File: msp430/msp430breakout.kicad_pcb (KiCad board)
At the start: 2 copper layers, 17 parts, among them P1 Power, X1 Power, X2 Power, X3 Left, X4 Power, X5 Power, X6 Right, X7 Debug

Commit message: a bit of work on the layout
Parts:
- added X8: PWR_L_OOL, Connector_PinHeader_2.54mm:PinHeader_2x02_P2.54mm_Vertical, B.Cu at (127.1, 101.3)
- added X9: PWR_R_OOL, Connector_PinHeader_2.54mm:PinHeader_2x02_P2.54mm_Vertical, B.Cu at (170.3, 101.3)
- C3: moved to B.Cu
- R1, R2: moved to F.Cu
- X3, X6: footprint Connector_PinHeader_2.54mm:PinHeader_1x06_P2.54mm_Vertical -> Connector_PinHeader_2.54mm:PinHeader_1x05_P2.54mm_Vertical
- X7: footprint Connector_Molex:Molex_Micro-Latch_53253-0370_1x03_P2.00mm_Vertical -> Connector_PinHeader_2.54mm:PinHeader_1x03_P2.54mm_Vertical
- moved R2 12.6 mm to (161.4, 98.7), turned to 270 degrees
- moved R1 12.5 mm to (161.4, 103.8), turned to 90 degrees
- moved R3 11.2 mm to (150.0, 104.0), turned to 0 degrees
- moved P1 8.25 mm to (150.0, 104.0), turned to 180 degrees
- moved R4 7.05 mm to (158.9, 98.7), turned to 90 degrees
- moved C2 6.53 mm to (142.4, 94.9), turned to 180 degrees
- moved X1 5.68 mm to (127.1, 94.9)
- moved X5 5.08 mm to (127.1, 105.1)
- moved X3 4.58 mm to (136.0, 94.9)
- moved X6 2.84 mm to (164.0, 94.9)
- moved X7 2.83 mm to (155.1, 94.9)
- moved C3 2.57 mm to (158.9, 97.5), turned to 0 degrees
- moved X2 2.54 mm to (170.3, 94.9)
- moved R5 2.36 mm to (156.3, 98.7), turned to 270 degrees
- moved C1 1.97 mm to (150.0, 96.0)
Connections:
- net SBWTDIO renamed NMI
- X6 pad 1: Net-(X6-Pad1) -> P2.7
- X6 pad 2: Net-(X6-Pad2) -> P2.6
- X6 pad 3: P2.7 -> P1.7
- X6 pad 4: P2.6 -> P1.6
- X6 pad 5: P1.7 -> P1.5
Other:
- board outline added: 50 x 14 mm
- board text added: "P1.0"
- board text added: "P1.1"
- board text added: "P1.2"
- board text added: "P1.3"
- board text added: "P1.4"
- board text added: "P1.5"
- board text added: "P1.6"
- board text added: "P1.7"
- board text added: "P2.6"
- board text added: "P2.7"

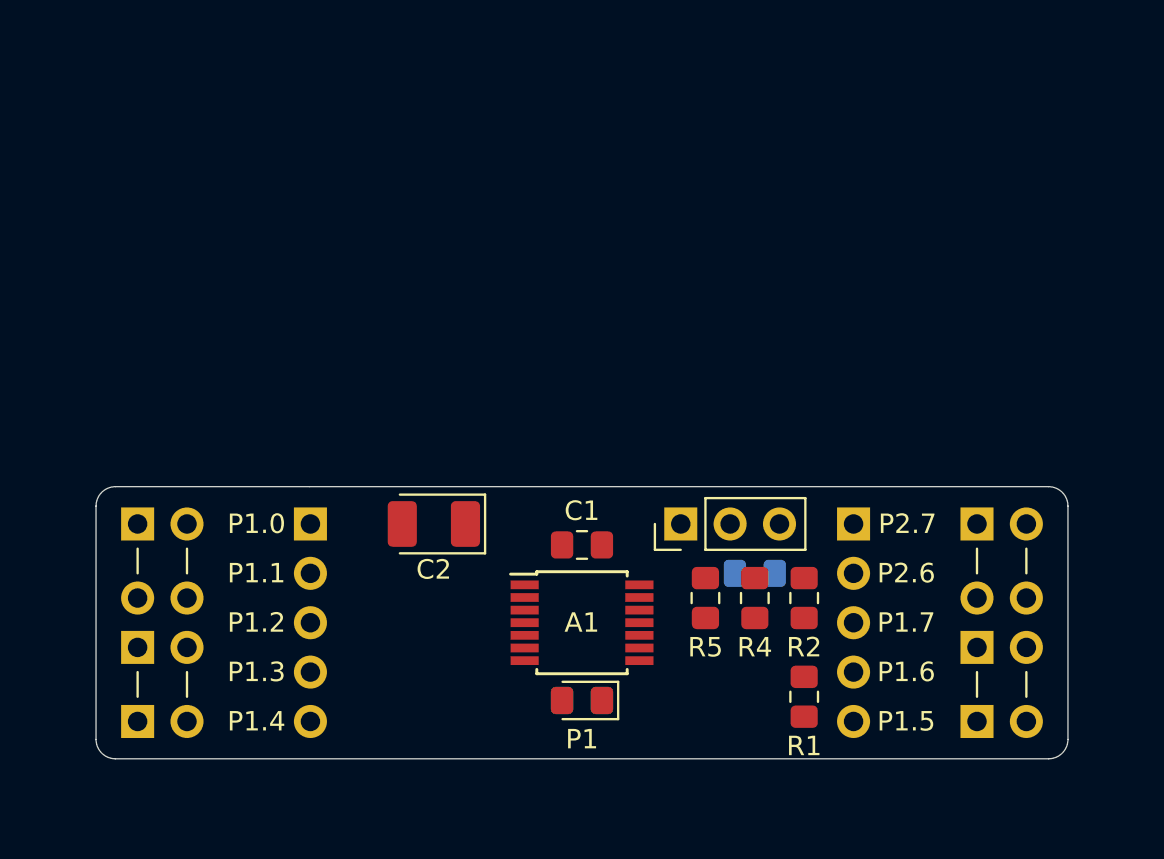
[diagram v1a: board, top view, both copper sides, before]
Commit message: increased board size to have planes go around pin headers
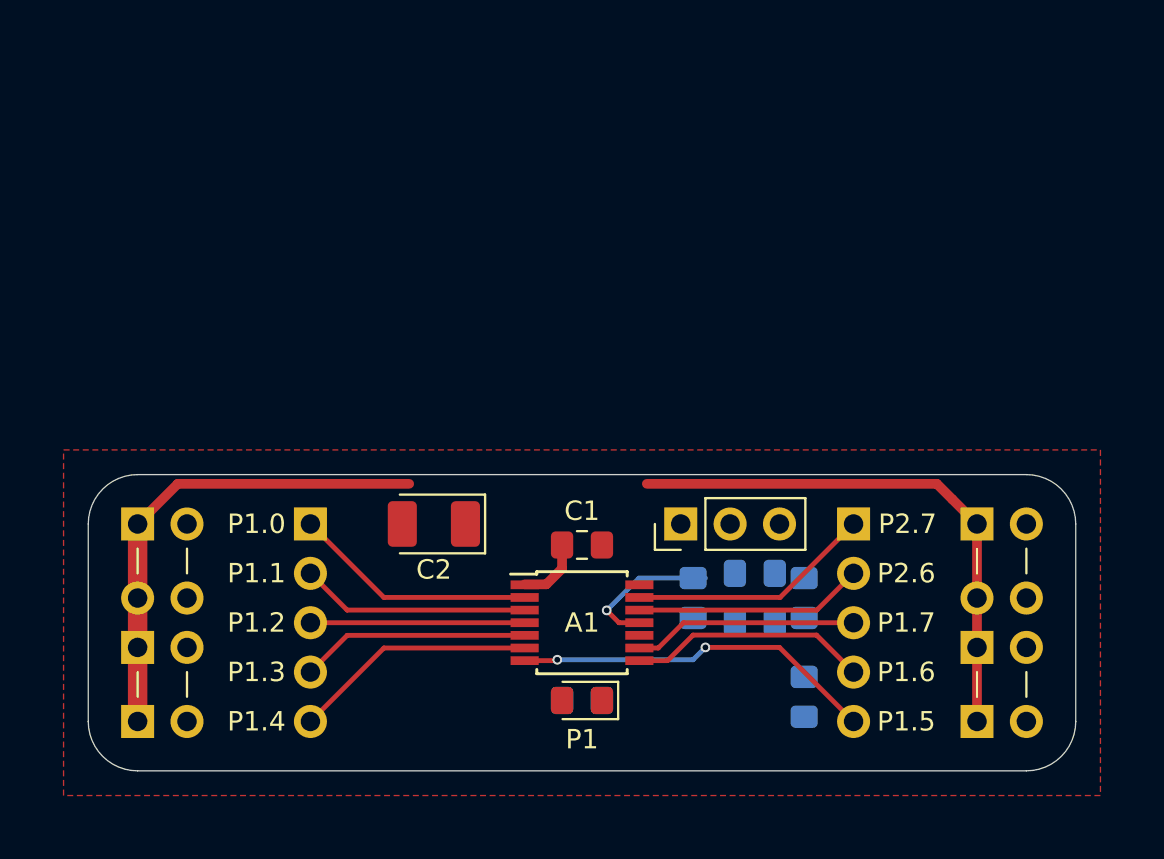
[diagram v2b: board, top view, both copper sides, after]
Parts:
- R1, R2, R4, R5: moved to B.Cu
- moved R4 1.27 mm to (158.9, 100.0), turned to 180 degrees
- moved R5 0.63 mm to (155.7, 98.7), turned to 90 degrees
- turned R1 to 270 degrees
- turned R2 to 90 degrees
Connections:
- net NMI renamed SBWTDIO
- X6 pad 1: P2.7 -> P2.6
- X6 pad 2: P2.6 -> P2.7
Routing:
- net VCC: track 0.00 -> 56.5 mm
- net P1.5: track 0.00 -> 18.8 mm, vias 0 -> 2
- net P2.6: track 0.00 -> 12.6 mm
- net P1.4: track 0.00 -> 12.6 mm
- net P1.0: track 0.00 -> 12.6 mm
- net P1.6: track 0.00 -> 12.4 mm
- net P2.7: track 0.00 -> 11.8 mm
- net P1.3: track 0.00 -> 11.8 mm
- net P1.1: track 0.00 -> 11.8 mm
- net P1.7: track 0.00 -> 11.6 mm
- net P1.2: track 0.00 -> 11.0 mm
- net SBWTCK: track 0.00 -> 7.71 mm, vias 0 -> 1
- added copper zone on F.Cu, net GND
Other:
- board size 50 x 14 mm -> 50.8 x 15.2 mm

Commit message: added linear regulator
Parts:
- added C4: 100n, Capacitor_SMD:C_0805_2012Metric_Pad1.15x1.40mm_HandSolder, B.Cu at (139.8, 97.5)
- added C5: ≥470n, Capacitor_SMD:C_0805_2012Metric_Pad1.15x1.40mm_HandSolder, B.Cu at (144.9, 97.5)
- added T1: TPS71433, Package_TO_SOT_SMD:SOT-353_SC-70-5, B.Cu at (142.4, 97.5)
- moved C2 7.65 mm to (150.0, 94.3), turned to 0 degrees
- moved R3 7.02 mm to (147.5, 97.5), turned to 90 degrees
- moved R4 3.42 mm to (155.7, 98.7), turned to 90 degrees
- moved R5 2.54 mm to (153.2, 98.7), turned to 270 degrees
- moved P1 2.35 mm to (150.0, 106.3)
- moved C1 1.46 mm to (150.0, 97.5)
- moved C3 1.42 mm to (158.3, 98.7), turned to 90 degrees
- moved A1 1.27 mm to (150.0, 101.3)
- moved R1 0.64 mm to (160.8, 103.8)
- moved R2 0.64 mm to (160.8, 98.7)
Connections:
- A1 pad 1: VCC -> VCCQ
- C1 pad 1: VCC -> VCCQ
- C2 pad 1: VCC -> VCCQ
- R1 pad 1: VCC -> VCCQ
- R2 pad 1: VCC -> VCCQ
- R3 pad 2: VCC -> VCCQ
- R4 pad 1: VCC -> VCCQ
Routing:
- net VCC: track 56.5 -> 20.3 mm
- net SBWTDIO: track 0.00 -> 14.9 mm, vias 0 -> 1
- net P1.5: track 18.8 -> 9.20 mm, vias 2 -> 1
- net Net-(P1-Pad2): track 0.00 -> 9.38 mm, vias 0 -> 1
- net GND: track 0.00 -> 8.99 mm
- net VCCQ: track 0.00 -> 8.90 mm, vias 0 -> 19
- net SBWTCK: track 7.71 -> 3.19 mm
- net P1.6: track 12.4 -> 16.5 mm
- net P1.7: track 11.6 -> 15.6 mm
- net Net-(R5-Pad1): track 0.00 -> 3.57 mm
- net P1.0: track 12.6 -> 13.9 mm
- net P1.3: track 11.8 -> 11.3 mm
- net P1.1: track 11.8 -> 12.3 mm
- net P1.2: track 11.0 -> 11.5 mm
- net P1.4: track 12.6 -> 12.1 mm
- added copper zone on B.Cu, net GND
- added copper zone on B.Cu, net VCC
- added copper zone on B.Cu, net VCCQ
- added copper zone on F.Cu, net VCCQ

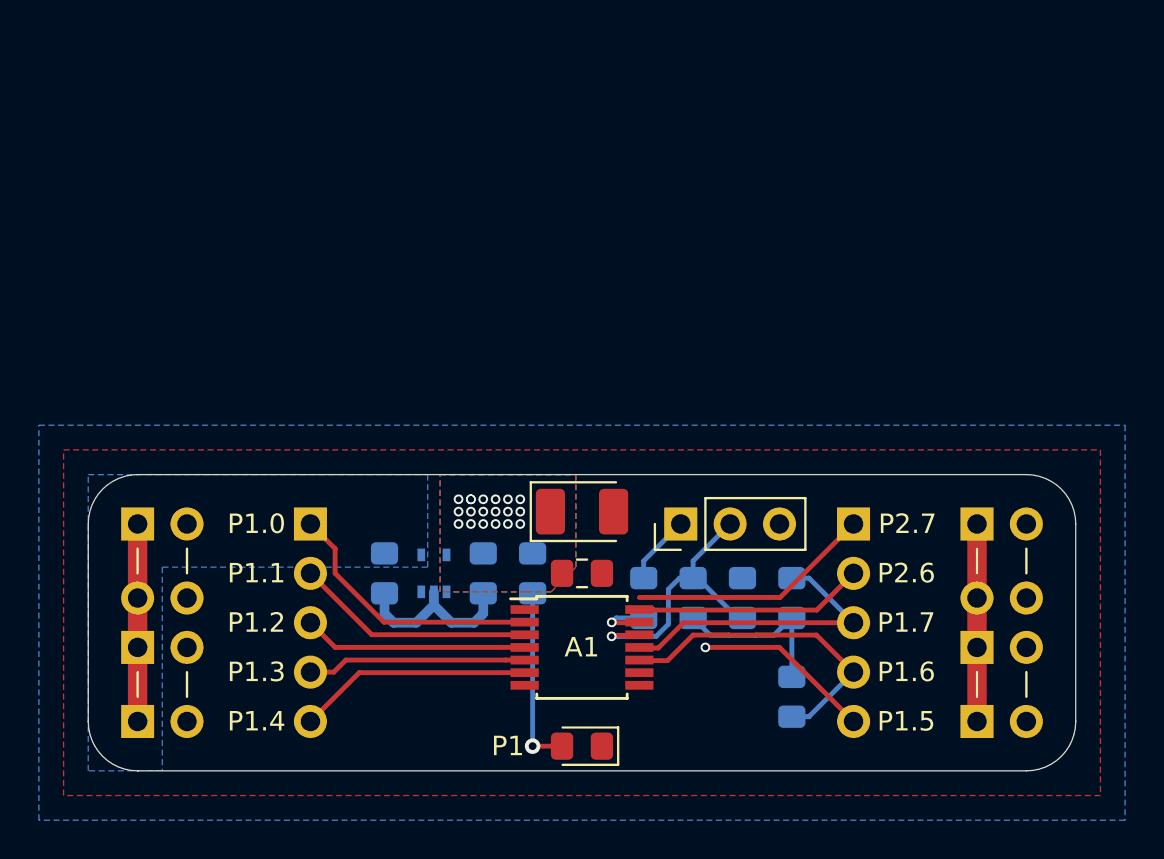
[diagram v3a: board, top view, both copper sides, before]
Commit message: modified for better usability with FET
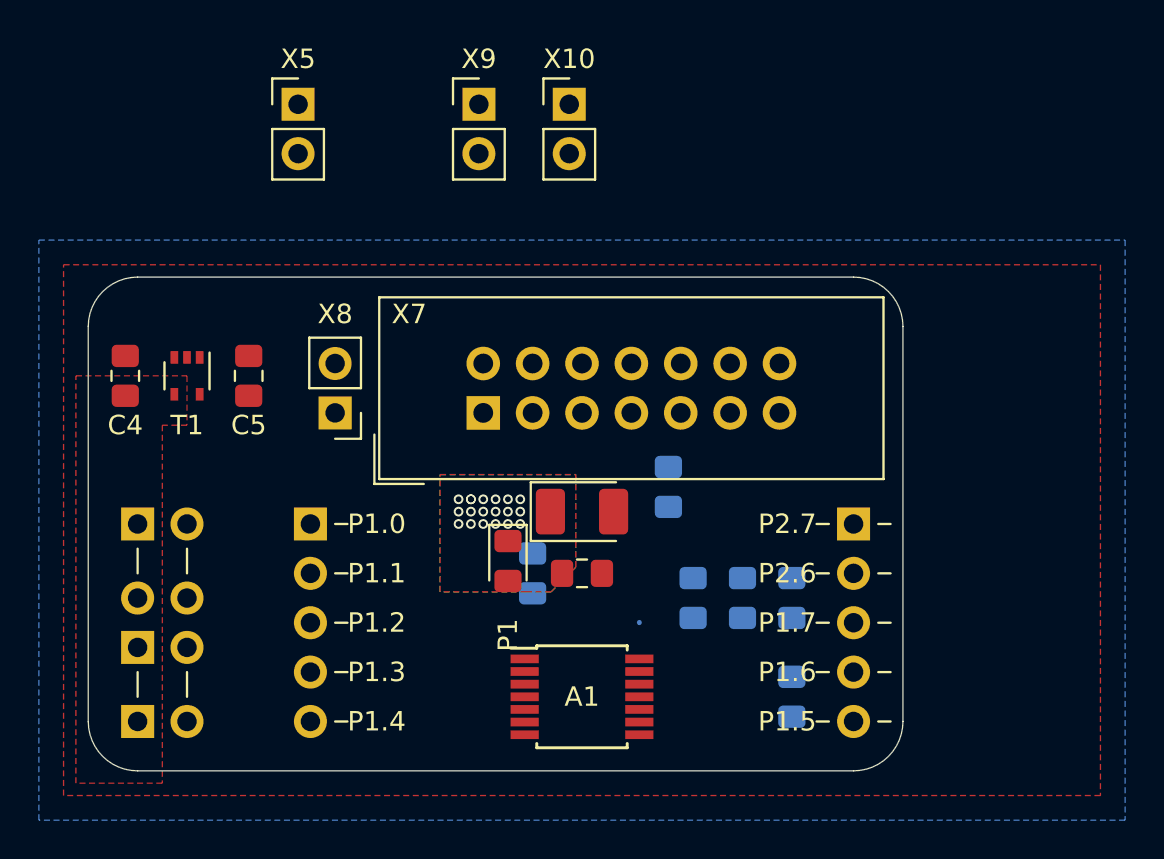
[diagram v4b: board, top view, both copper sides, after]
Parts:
- removed the X4 at (170.3, 105.1)
- added X10: backchannel UART, Connector_PinHeader_2.54mm:PinHeader_1x02_P2.54mm_Vertical, F.Cu at (149.3, 73.3)
- added X8: power by tool, Connector_PinHeader_2.54mm:PinHeader_1x02_P2.54mm_Vertical, F.Cu at (137.3, 89.2)
- C4, C5, T1: moved to F.Cu
- X1, X2: value Power -> power
- X4: renamed from X8; value PWR_L_OOL -> power
- X5: value Power -> bus is 3.3V; moved to F.Cu
- X7: value Debug -> Spy-Bi-Wire; footprint Connector_PinHeader_2.54mm:PinHeader_1x03_P2.54mm_Vertical -> Connector_IDC:IDC-Header_2x07_P2.54mm_Vertical
- X9: value PWR_R_OOL -> backchannel UART; footprint Connector_PinHeader_2.54mm:PinHeader_2x02_P2.54mm_Vertical -> Connector_PinHeader_2.54mm:PinHeader_1x02_P2.54mm_Vertical; moved to F.Cu
- moved X2 44.4 mm to (127.1, 105.1)
- moved X9 37.9 mm to (144.7, 73.3)
- moved X5 32.8 mm to (135.4, 73.3), turned to 0 degrees
- moved C4 16.8 mm to (126.5, 87.3), turned to 90 degrees
- moved T1 16.3 mm to (129.7, 87.3), turned to 270 degrees
- moved C5 15.8 mm to (132.9, 87.3), turned to 90 degrees
- moved X7 11.7 mm to (144.9, 89.2)
- moved P1 10.3 mm to (146.2, 96.8), turned to 270 degrees
- moved R5 5.85 mm to (154.4, 93.0)
- moved A1 2.54 mm to (150.0, 103.8)
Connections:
- A1 pad 1: VCCQ -> VCC
- C1 pad 1: VCCQ -> VCC
- C2 pad 1: VCCQ -> VCC
- C4 pad 1: VCC -> +5V
- C5 pad 1: VCCQ -> VCC
- R1 pad 1: VCCQ -> VCC
- R2 pad 1: VCCQ -> VCC
- R3 pad 2: VCCQ -> VCC
- R4 pad 1: VCCQ -> VCC
- T1 pad 4: VCC -> +5V
- T1 pad 5: VCCQ -> VCC
- X1 pad 1: VCC -> +5V
- X2 pad 1: VCC -> +5V
- X4 pad 1: VCC -> +5V
- X4 pad 3: VCC -> +5V
- X5 pad 1: VCC -> +5V
- X5 pad 2: GND -> VCC
- X7 pad 1: Net-(R5-Pad1) -> SBWTDIO
- X7 pad 2: SBWTDIO -> +3V3
- X7 pad 3: GND -> Net-(X7-Pad3)
- X9 pad 1: VCC -> Net-(X9-Pad1)
- X9 pad 2: GND -> UART_TXD
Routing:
- net VCC: track 20.3 -> 0.00 mm, vias 0 -> 19
- net P1.6: track 16.5 -> 0.00 mm
- net P1.7: track 15.6 -> 0.00 mm
- net SBWTDIO: track 14.9 -> 0.00 mm, vias 1 -> 0
- net P1.0: track 13.9 -> 0.00 mm
- net P2.6: track 12.6 -> 0.00 mm
- net P1.1: track 12.3 -> 0.00 mm
- net P1.4: track 12.1 -> 0.00 mm
- net P2.7: track 11.8 -> 0.00 mm
- net P1.2: track 11.5 -> 0.00 mm
- net P1.3: track 11.3 -> 0.00 mm
- net Net-(P1-Pad2): track 9.38 -> 0.00 mm, vias 1 -> 0
- net P1.5: track 9.20 -> 0.00 mm, vias 1 -> 0
- net GND: track 8.99 -> 0.00 mm
- net VCCQ: track 8.90 -> 0.00 mm, vias 19 -> 0
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- added copper zone on F.Cu, net +5V
- added copper zone on F.Cu, net VCC
- removed copper zone on B.Cu, net VCCQ
- removed copper zone on F.Cu, net VCCQ
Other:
- board size 50.8 x 15.2 mm -> 41.9 x 25.4 mm

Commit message: finished rev.0
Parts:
- removed the C3 at (158.3, 98.7)
- removed the C4 at (126.5, 87.3)
- removed the R1 at (160.8, 103.8)
- removed R4: 47k, Resistor_SMD:R_0805_2012Metric_Pad1.15x1.40mm_HandSolder
- removed R5: 330, Resistor_SMD:R_0805_2012Metric_Pad1.15x1.40mm_HandSolder
- removed X10: backchannel UART, Connector_PinHeader_2.54mm:PinHeader_1x02_P2.54mm_Vertical
- removed the X5 at (135.4, 73.3)
- added C1: 100 nF, Capacitor_SMD:C_0805_2012Metric_Pad1.15x1.40mm_HandSolder, F.Cu at (126.5, 87.3)
- added C5: 2.2 nF, Capacitor_SMD:C_0805_2012Metric_Pad1.15x1.40mm_HandSolder, F.Cu at (143.0, 94.9)
- added QR*****: QR_AISLER, local:QR_AISLER, B.Cu at (144.9, 100.0)
- added R3: 330, Resistor_SMD:R_0805_2012Metric_Pad1.15x1.40mm_HandSolder, F.Cu at (154.4, 94.9)
- added X8: backchannel UART, Resistor_SMD:R_0805_2012Metric_Pad1.15x1.40mm_HandSolder, F.Cu at (157.0, 94.9)
- C2: renamed from C5; value ≥470n -> ≥470 nF
- C3: renamed from C1; value 100n -> 100 nF
- C4: renamed from C2; value 10µ, 10 V -> 10 µF, 10 V
- R1: renamed from R3; moved to F.Cu
- R2: value R -> 47k; moved to F.Cu
- X9: footprint Connector_PinHeader_2.54mm:PinHeader_1x02_P2.54mm_Vertical -> Resistor_SMD:R_0805_2012Metric_Pad1.15x1.40mm_HandSolder
- moved X9 26.2 mm to (159.5, 94.9), turned to 90 degrees
- moved R2 15.7 mm to (145.6, 94.9)
- moved R1 14.6 mm to (132.9, 97.5)
- moved P1 14.1 mm to (132.9, 92.4), turned to 90 degrees
- moved X7 3.24 mm to (136.7, 86.0), turned to 0 degrees
- moved C3 2.54 mm to (150.0, 100.0)
- moved C4 2.54 mm to (150.0, 96.8)
- renumbered X4 to X3, X3 to X4, X6 to X5, X7 to X6, X8 to X7
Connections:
- P1 pad 1: GND -> Net-(P1-Pad1)
- P1 pad 2: Net-(P1-Pad2) -> VCC
- R1 pad 1: Net-(P1-Pad2) -> GND
- R1 pad 2: VCC -> Net-(P1-Pad1)
- R2 pad 2: P1.7 -> SBWTDIO
- X9 pad 1: Net-(X9-Pad1) -> P1.1
- X9 pad 2: UART_TXD -> UART_RXD
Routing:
- net P1.1: track 0.00 -> 34.8 mm, vias 0 -> 2
- net P1.2: track 0.00 -> 31.8 mm, vias 0 -> 2
- net SBWTDIO: track 0.00 -> 22.9 mm, vias 0 -> 2
- net P1.5: track 0.00 -> 17.7 mm
- net P2.6: track 0.00 -> 14.2 mm
- net P1.0: track 0.00 -> 14.2 mm
- net P2.7: track 0.00 -> 13.4 mm
- net P1.7: track 0.00 -> 13.1 mm
- net P1.6: track 0.00 -> 12.4 mm
- net P1.3: track 0.00 -> 11.8 mm
- net P1.4: track 0.00 -> 11.0 mm
- net SBWTCK: track 0.02 -> 9.70 mm, vias 0 -> 2
- net +3V3: track 0.00 -> 8.52 mm
- net UART_TXD: track 0.00 -> 8.02 mm
- net UART_RXD: track 0.00 -> 8.02 mm
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- removed copper zone on B.Cu, net VCC
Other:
- board text added: "RX"
- board text added: "TX"
- board text added: "rev. 0"
- board text removed: "P2.6"
- board text removed: "P2.7"
